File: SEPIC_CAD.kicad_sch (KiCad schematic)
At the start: 25 parts, among them IC1 LM5155DSSR, Q1 CSD18537NQ5A

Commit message: checking issues
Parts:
- D1: footprint D2PAK_STM -> Global Libraries:STPS20M100SG-TR
- IC1: footprint SON50P200X300X80-13N-D -> Global Libraries:SON50P200X300X80-13N-D
- L1: footprint (none) -> Global Libraries:WE-DD_12XX_CROSSED12
- Q1: footprint CSD19531Q5AT -> Global Libraries:CSD19531Q5AT
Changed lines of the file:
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@@
       (effects (font (size 1.27 1.27)) (justify left))
     )
-    (property "Footprint" "CSD19531Q5AT" (id 2) (at 180.34 74.93 0)
-      (effects (font (size 1.27 1.27)) (justify left) hide)
+    (property "Footprint" "Global Libraries:CSD19531Q5AT" (id 2) (at 180.34 74.93 0)
+      (effects (font (size 1.27 1.27)) (justify left))
     )
     (property "Datasheet" "http://www.ti.com/lit/gpn/csd18537nq5a" (id 3) (at 177.8 74.93 0)
@@
       (effects (font (size 1.27 1.27)) (justify right))
     )
-    (property "Value" "34k8" (id 1) (at 81.28 67.31 0)
+    (property "Value" "34k8" (id 1) (at 80.01 67.31 0)
       (effects (font (size 1.27 1.27)) (justify right))
     )
@@
     (property "Reference" "IC1" (id 0) (at 116.84 62.23 0))
     (property "Value" "LM5155DSSR" (id 1) (at 116.84 64.77 0))
-    (property "Footprint" "SON50P200X300X80-13N-D" (id 2) (at 139.7 76.2 0)
+    (property "Footprint" "Global Libraries:SON50P200X300X80-13N-D" (id 2) (at 139.7 76.2 0)
       (effects (font (size 1.27 1.27)) (justify left) hide)
     )
@@
       (effects (font (size 1.524 1.524)))
     )
-    (property "Footprint" "D2PAK_STM" (id 2) (at 197.485 92.964 0)
+    (property "Footprint" "Global Libraries:STPS20M100SG-TR" (id 2) (at 197.485 92.964 0)
       (effects (font (size 1.524 1.524)) hide)
     )
@@
       (effects (font (size 1.27 1.27)) (justify right))
     )
-    (property "Footprint" "" (id 2) (at 176.53 59.69 0)
+    (property "Footprint" "Global Libraries:WE-DD_12XX_CROSSED12" (id 2) (at 176.53 59.69 0)
       (effects (font (size 1.27 1.27)) hide)
     )
@@
     )
     (path "/b910f5a9-203b-4617-b055-34ba181d7395"
-      (reference "D1") (unit 1) (value "STPS20M100SG-TR") (footprint "D2PAK_STM")
+      (reference "D1") (unit 1) (value "STPS20M100SG-TR") (footprint "Global Libraries:STPS20M100SG-TR")
     )
     (path "/899f4c1a-985b-472e-a9b0-465d356ef34c"
-      (reference "IC1") (unit 1) (value "LM5155DSSR") (footprint "SON50P200X300X80-13N-D")
+      (reference "IC1") (unit 1) (value "LM5155DSSR") (footprint "Global Libraries:SON50P200X300X80-13N-D")
     )
     (path "/ec620b77-8919-4285-a6c0-f21b0acac14b"
-      (reference "L1") (unit 1) (value "7448700015") (footprint "")
+      (reference "L1") (unit 1) (value "7448700015") (footprint "Global Libraries:WE-DD_12XX_CROSSED12")
     )
     (path "/2097c02a-9419-426d-a010-cdecd44e7e36"
-      (reference "Q1") (unit 1) (value "CSD18537NQ5A") (footprint "CSD19531Q5AT")
+      (reference "Q1") (unit 1) (value "CSD18537NQ5A") (footprint "Global Libraries:CSD19531Q5AT")
     )
     (path "/df5d2842-95e0-4dc7-91e0-af6aa7f859bb"

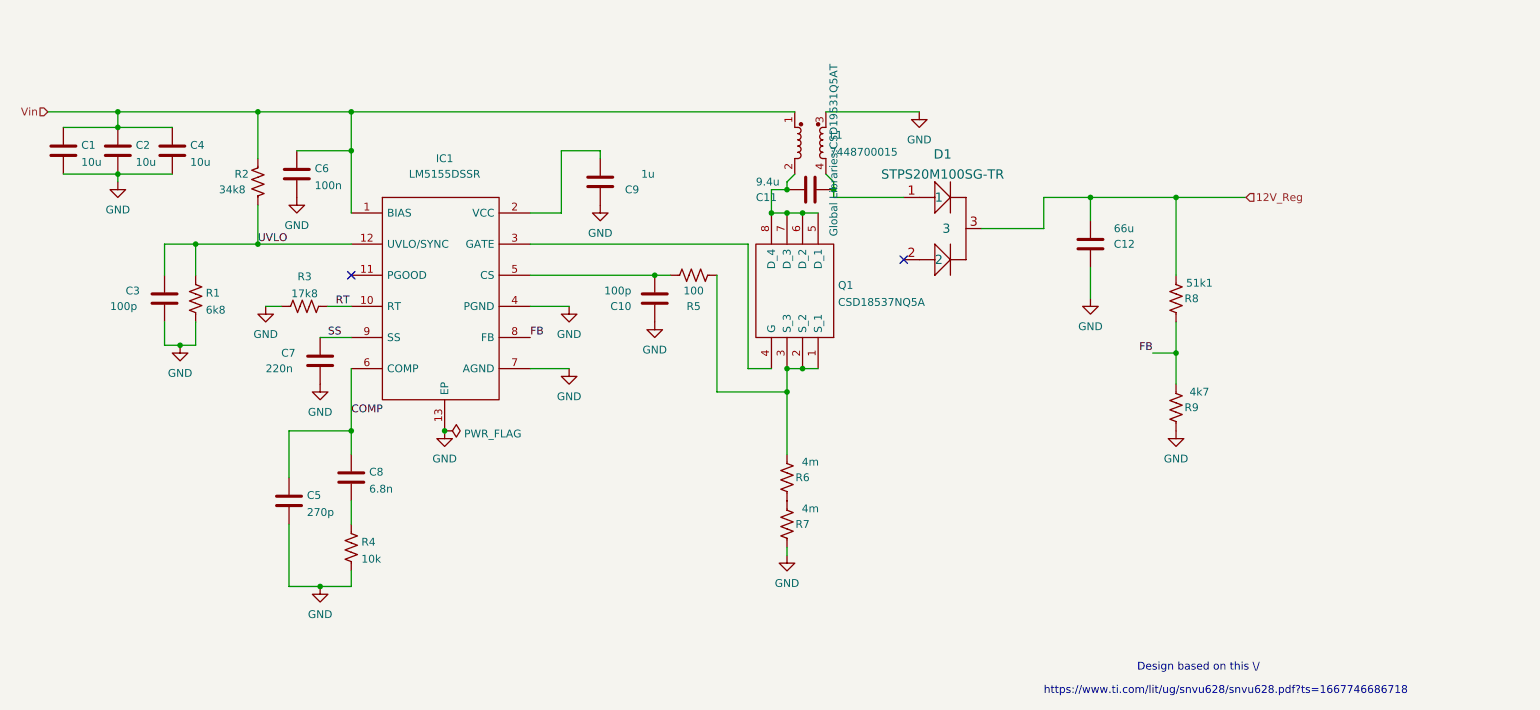
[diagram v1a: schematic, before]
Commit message: adjusted cap values
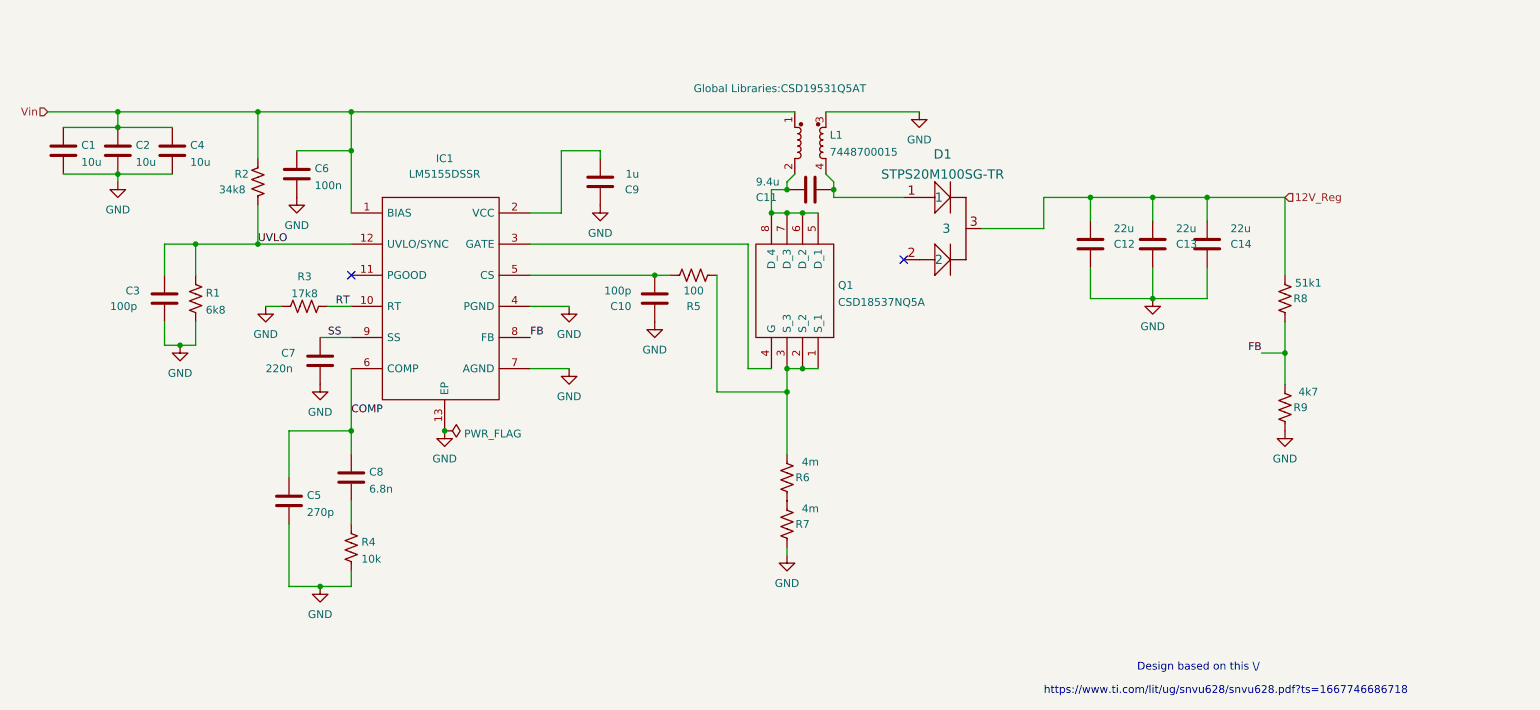
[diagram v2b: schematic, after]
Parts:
- added C13, C14: 22u, Capacitor_SMD:C_0603_1608Metric_Pad1.08x0.95mm_HandSolder, symbol Device:C
- C1, C10, C11, C2, C3, C4, C5, C6, C7, C8, C9: footprint (none) -> Capacitor_SMD:C_0603_1608Metric_Pad1.08x0.95mm_HandSolder
- C12: value 66u -> 22u; footprint (none) -> Capacitor_SMD:C_0603_1608Metric_Pad1.08x0.95mm_HandSolder
- R1, R2, R3, R4, R5, R6, R7, R8, R9: footprint (none) -> Resistor_SMD:R_0603_1608Metric_Pad0.98x0.95mm_HandSolder
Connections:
- net 12V_Reg: now also C13.1, C14.1
- net GND: now also C13.2, C14.2
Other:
- moved on the sheet: R8, R9
